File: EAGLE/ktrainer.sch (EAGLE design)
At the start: 10 parts

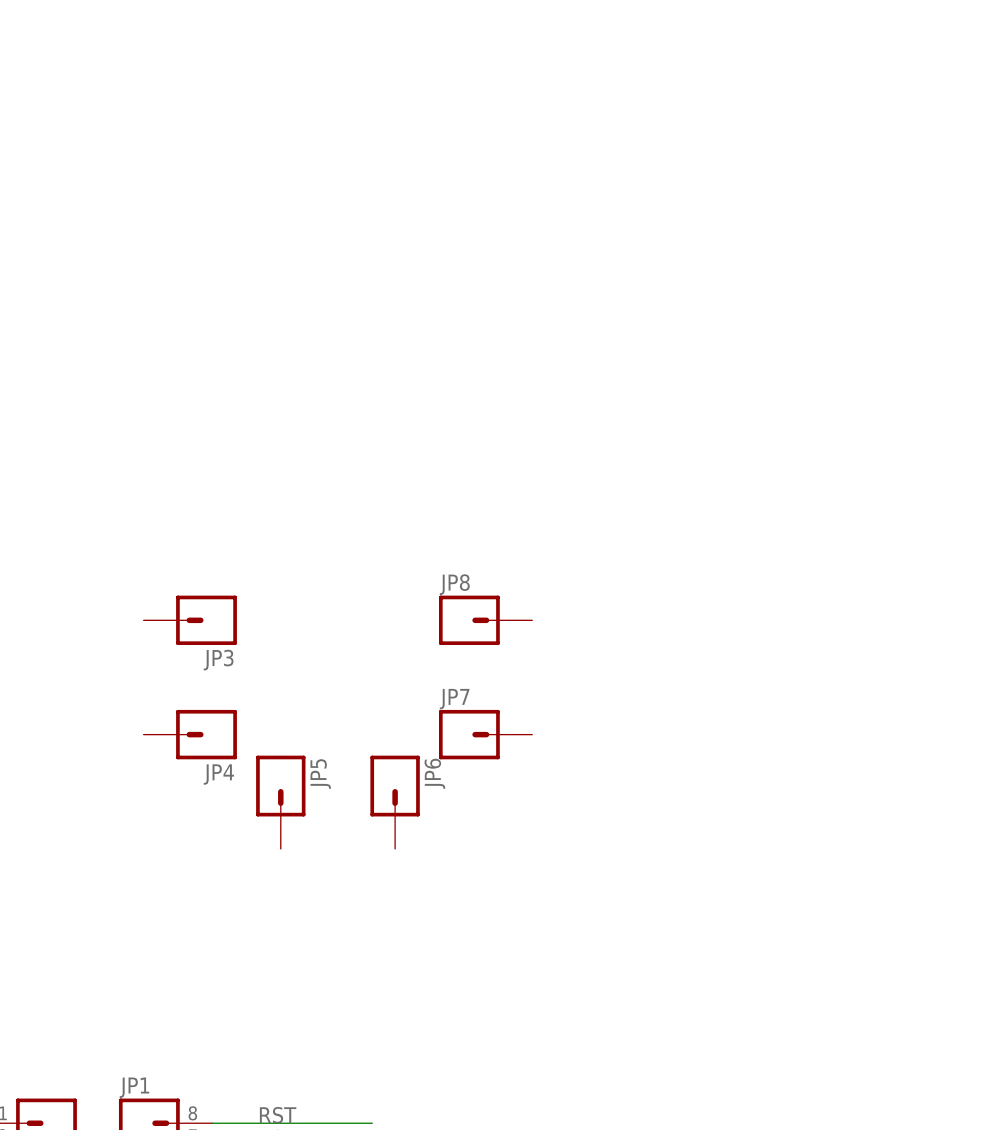
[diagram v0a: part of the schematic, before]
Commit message: First thoughts on the physical layout of buttons & screen
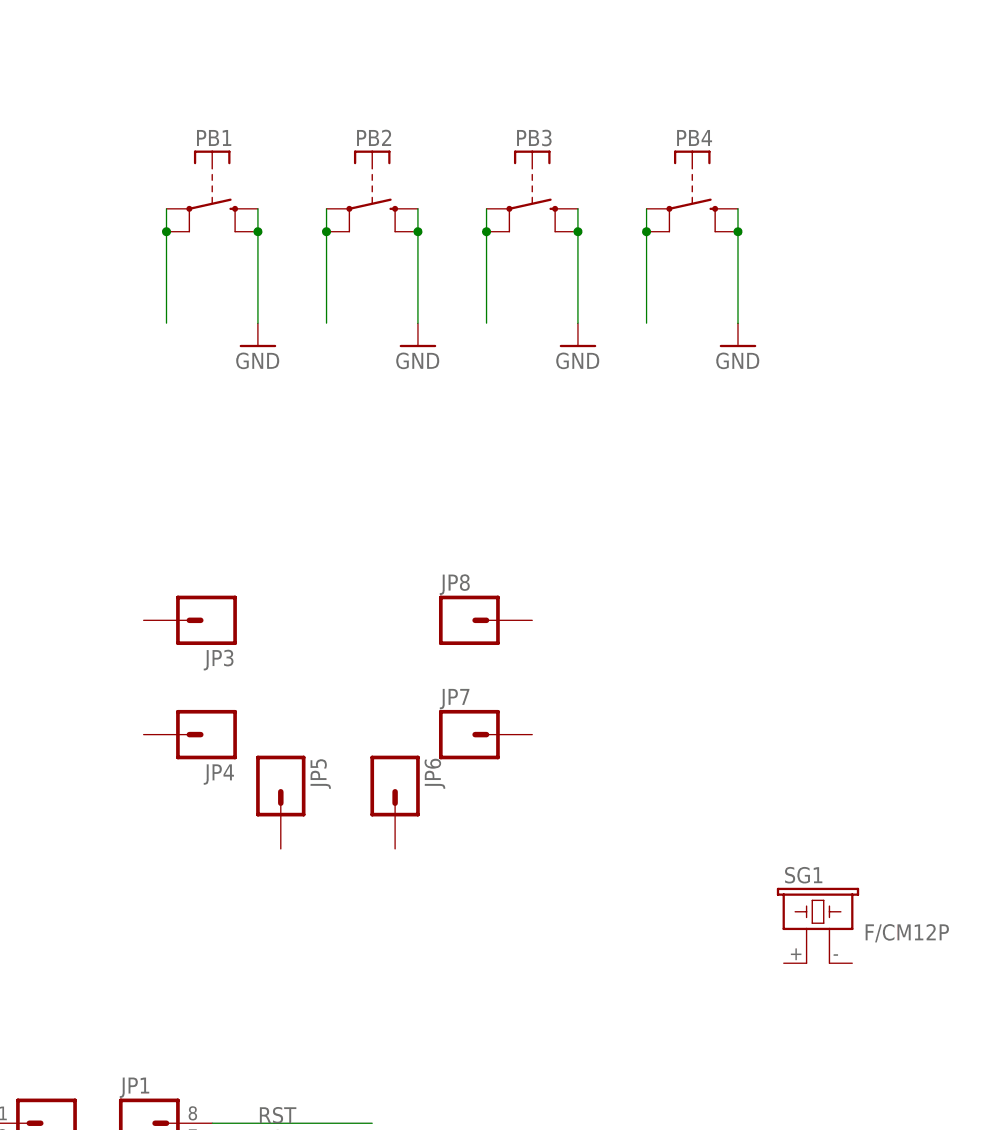
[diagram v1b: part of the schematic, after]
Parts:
- added PB1, PB2, PB3, PB4: SWITCH-SKRA, formatc1702-switches:SWITCH-SKRA
- added SG1: F/CM12P, buzzer:F/CM12P
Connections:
- new net N$1: PB1.S, PB1.S@1
- new net N$2: PB2.S, PB2.S@1
- new net N$3: PB3.S, PB3.S@1
- new net N$4: PB4.S, PB4.S@1
- net GND: now also PB1.P, PB1.P@1, PB2.P, PB2.P@1, PB3.P, PB3.P@1, PB4.P, PB4.P@1
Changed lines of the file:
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@@
 <?xml version="1.0" encoding="utf-8"?>
 <!DOCTYPE eagle SYSTEM "eagle.dtd">
-<eagle version="7.4.0">
+<eagle version="6.5.0">
 <drawing>
 <settings>
@@
 <part name="JP8" library="SparkFun-Connectors" deviceset="M01" device="NOSILK-KIT"/>
 <part name="JP9" library="SparkFun-Connectors" deviceset="M01" device="NOSILK-KIT"/>
+<part name="PB1" library="formatc1702-switches" deviceset="SWITCH-SKRA" device=""/>
+<part name="PB2" library="formatc1702-switches" deviceset="SWITCH-SKRA" device=""/>
+<part name="PB3" library="formatc1702-switches" deviceset="SWITCH-SKRA" device=""/>
+<part name="PB4" library="formatc1702-switches" deviceset="SWITCH-SKRA" device=""/>
+<part name="GND1" library="supply1" deviceset="GND" device=""/>
+<part name="GND2" library="supply1" deviceset="GND" device=""/>
+<part name="GND3" library="supply1" deviceset="GND" device=""/>
+<part name="GND4" library="supply1" deviceset="GND" device=""/>
+<part name="SG1" library="buzzer" deviceset="F/CM12P" device=""/>
 </parts>
 <sheets>
@@
 <attribute name="VALUE" x="43.18" y="58.42" size="1.778" layer="96" rot="R180"/>
 </instance>
+<instance part="PB1" gate="G$1" x="58.42" y="182.88"/>
+<instance part="PB2" gate="G$1" x="76.2" y="182.88"/>
+<instance part="PB3" gate="G$1" x="93.98" y="182.88"/>
+<instance part="PB4" gate="G$1" x="111.76" y="182.88"/>
+<instance part="GND1" gate="1" x="63.5" y="167.64"/>
+<instance part="GND2" gate="1" x="81.28" y="167.64"/>
+<instance part="GND3" gate="1" x="99.06" y="167.64"/>
+<instance part="GND4" gate="1" x="116.84" y="167.64"/>
+<instance part="SG1" gate="G$1" x="124.46" y="101.6"/>
 </instances>
 <busses>
@@
 <label x="20.32" y="66.04" size="1.778" layer="95"/>
 </segment>
+<segment>
+<pinref part="PB1" gate="G$1" pin="P"/>
+<wire x1="63.5" y1="182.88" x2="63.5" y2="180.34" width="0.1524" layer="91"/>
+<pinref part="GND1" gate="1" pin="GND"/>
+<pinref part="PB1" gate="G$1" pin="P@1"/>
+<wire x1="63.5" y1="180.34" x2="63.5" y2="170.18" width="0.1524" layer="91"/>
+<junction x="63.5" y="180.34"/>
+</segment>
+<segment>
+<pinref part="PB2" gate="G$1" pin="P"/>
+<wire x1="81.28" y1="182.88" x2="81.28" y2="180.34" width="0.1524" layer="91"/>
+<pinref part="GND2" gate="1" pin="GND"/>
+<pinref part="PB2" gate="G$1" pin="P@1"/>
+<wire x1="81.28" y1="180.34" x2="81.28" y2="170.18" width="0.1524" layer="91"/>
+<junction x="81.28" y="180.34"/>
+</segment>
+<segment>
+<pinref part="PB3" gate="G$1" pin="P"/>
+<wire x1="99.06" y1="182.88" x2="99.06" y2="180.34" width="0.1524" layer="91"/>
+<pinref part="GND3" gate="1" pin="GND"/>
+<pinref part="PB3" gate="G$1" pin="P@1"/>
+<wire x1="99.06" y1="180.34" x2="99.06" y2="170.18" width="0.1524" layer="91"/>
+<junction x="99.06" y="180.34"/>
+</segment>
+<segment>
+<pinref part="PB4" gate="G$1" pin="P"/>
+<wire x1="116.84" y1="182.88" x2="116.84" y2="180.34" width="0.1524" layer="91"/>
+<pinref part="GND4" gate="1" pin="GND"/>
+<pinref part="PB4" gate="G$1" pin="P@1"/>
+<wire x1="116.84" y1="180.34" x2="116.84" y2="170.18" width="0.1524" layer="91"/>
+<junction x="116.84" y="180.34"/>
+</segment>
 </net>
 <net name="D4" class="0">
@@
 </segment>
 </net>
+<net name="N$1" class="0">
+<segment>
+<pinref part="PB1" gate="G$1" pin="S"/>
+<wire x1="53.34" y1="182.88" x2="53.34" y2="180.34" width="0.1524" layer="91"/>
+<pinref part="PB1" gate="G$1" pin="S@1"/>
+<wire x1="53.34" y1="180.34" x2="53.34" y2="170.18" width="0.1524" layer="91"/>
+<junction x="53.34" y="180.34"/>
+</segment>
+</net>
+<net name="N$2" class="0">
+<segment>
+<pinref part="PB2" gate="G$1" pin="S"/>
+<wire x1="71.12" y1="182.88" x2="71.12" y2="180.34" width="0.1524" layer="91"/>
+<pinref part="PB2" gate="G$1" pin="S@1"/>
+<wire x1="71.12" y1="180.34" x2="71.12" y2="170.18" width="0.1524" layer="91"/>
+<junction x="71.12" y="180.34"/>
+</segment>
+</net>
+<net name="N$3" class="0">
+<segment>
+<pinref part="PB3" gate="G$1" pin="S"/>
+<wire x1="88.9" y1="182.88" x2="88.9" y2="180.34" width="0.1524" layer="91"/>
+<pinref part="PB3" gate="G$1" pin="S@1"/>
+<wire x1="88.9" y1="180.34" x2="88.9" y2="170.18" width="0.1524" layer="91"/>
+<junction x="88.9" y="180.34"/>
+</segment>
+</net>
+<net name="N$4" class="0">
+<segment>
+<pinref part="PB4" gate="G$1" pin="S"/>
+<wire x1="106.68" y1="182.88" x2="106.68" y2="180.34" width="0.1524" layer="91"/>
+<pinref part="PB4" gate="G$1" pin="S@1"/>
+<wire x1="106.68" y1="180.34" x2="106.68" y2="170.18" width="0.1524" layer="91"/>
+<junction x="106.68" y="180.34"/>
+</segment>
+</net>

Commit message: Work on schematic/PCB (not finished)
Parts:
- removed JP1_1: (no value), SparkFun-Connectors:M08NO_SILK_FEMALE_PTH
- removed JP2: OLED, SparkFun-Connectors:M04LONGPADS
- removed JP3, JP4, JP5, JP6, JP7, JP8, JP9: (no value), SparkFun-Connectors:M01NOSILK-KIT
- removed SG1: F/CM12P, buzzer:F/CM12P
- added BUZ1: F/CM12P, buzzer:F/CM12P
- added C1, C2: (no value), rcl:C-EUC0805
- added H1, H2, H3, H4: MOUNT-HOLE2.8, holes:MOUNT-HOLE2.8
- added IC1: DS3231/SO, adafruit:DS3231/SO
- added JP10: POLOLU step up/down 3V3, SparkFun-Connectors:M04LONGPADS
- added LED1: WS2812B, WS2812B:WS2812B
- added R1, R2: (no value), rcl:R-EU_R0805
- added S1: (no value), adafruit:EG1218S
- added SJ1: (no value), jumper:SJ2W
- added U$1: TP4056-LIPO-CHG-PCB, formatc1702-pcbs:TP4056-LIPO-CHG-PCB
- added U$2: SSD1306-OLED-128X64-I2C, formatc1702-pcbs:SSD1306-OLED-128X64-I2C
- added UC1: Wemos D1 mini Pro, esp8266modules:WEMOS-D1-MINI
- JP1: value Wemos D1 mini pro -> (none); device SparkFun-Connectors:M08NO_SILK_FEMALE_PTH -> pinhead:PINHD-1X2
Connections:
- removed net 3V3: JP1.1
- removed net 5V_USB: JP9.1
- removed net A0: JP1.7
- removed net D0: JP1.6
- removed net D1: JP1_1.3
- removed net D2: JP1_1.4
- removed net D3: JP1_1.5
- removed net D4: JP1_1.6
- removed net D5: JP1.5
- removed net D6: JP1.4
- removed net D7: JP1.3
- removed net D8: JP1.2
- removed net N$1: PB1.S, PB1.S@1
- removed net N$2: PB2.S, PB2.S@1
- removed net N$3: PB3.S, PB3.S@1
- removed net N$4: PB4.S, PB4.S@1
- removed net RST: JP1.8
- removed net RX: JP1_1.2
- removed net TX: JP1_1.1
- removed net V_IN: JP1_1.8
- new net +3V3: C1.1, IC1.VCC, JP10.1, LED1.VDD, U$2.VCC, UC1.3V3
- new net +5V: U$1.IN+, UC1.5V
- new net BATSENS: R1.1, R2.2, UC1.A0
- new net BUZZER: BUZ1.1, UC1.D7
- new net LED: LED1.DI, UC1.D6
- new net N$5: JP1.1, U$1.B+
- new net N$6: JP1.2, U$1.B-
- new net N$7: C2.1, IC1.VBAT, SJ1.2
- new net N$8: JP10.3, S1.S
- new net PB1: PB1.S, PB1.S@1, UC1.D1
- new net PB2: PB2.S, PB2.S@1, UC1.D2
- new net PB3: PB3.S, PB3.S@1, UC1.D3
- new net PB4: PB4.S, PB4.S@1, UC1.D4
- new net SCL: IC1.SCL, U$2.SCL, UC1.D5
- new net SDA: IC1.SDA, U$2.SDA, UC1.D0
- new net SHDN: JP10.4
- new net VCC: R1.2, S1.P, U$1.OUT+
- net GND: now also BUZ1.2, C1.2, C2.2, IC1.GND, JP10.2, LED1.GND, R2.1, SJ1.3, U$1.IN-, U$1.OUT-, U$2.GND, UC1.GND; no longer JP1_1.7

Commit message: More work on schematic/PCB (not finished)
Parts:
- removed BUZ1: F/CM12P, buzzer:F/CM12P
- removed H1, H2, H3, H4: MOUNT-HOLE2.8, holes:MOUNT-HOLE2.8
- removed JP10: POLOLU step up/down 3V3, SparkFun-Connectors:M04LONGPADS
- added BUZ+, BUZ-: (no value), wirepad:SMD2
- added JP2: (no value), pinhead:PINHD-1X2
- added U$3: POLOLU-S7V8F3-3V3-STEP-UP-DOWN, formatc1702-pcbs:POLOLU-S7V8F3-3V3-STEP-UP-DOWN
- C1, C2: value (none) -> 100n
- S1: value (none) -> SWITCH-MSK12D04-SLIDER-SMD; device adafruit:EG1218S -> formatc1702-switches:SWITCH-MSK12D04-SLIDER-SMD
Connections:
- net N$7 renamed VBAT
- removed net BUZZER: BUZ1.1, UC1.D7
- removed net N$5: JP1.1, U$1.B+
- removed net SHDN: JP10.4
- new net AUX: JP2.1, UC1.D1
- new net BUZ: BUZ+.P, UC1.D0
- net +3V3: now also U$3.VOUT; no longer JP10.1
- net GND: now also BUZ-.P, JP2.2, U$3.GND; no longer BUZ1.2, JP10.2
- net LED: now also UC1.D4; no longer UC1.D6
- net N$8: now also S1.O, U$3./SHDN, U$3.VIN; no longer JP10.3, S1.S
- net PB1: now also UC1.D7; no longer UC1.D1
- net PB2: now also UC1.D8; no longer UC1.D2
- net PB4: now also UC1.D2; no longer UC1.D4
- net SCL: now also UC1.D6; no longer UC1.D5
- net SDA: now also UC1.D5; no longer UC1.D0
- net VCC: now also JP1.1, SJ1.1, U$1.B+
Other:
- note added: "RETHINK THIS... Remove Wemos regulator? OUTDATED: Cut D2 diode on Wemos D1 mini pro (between VBUS (USB) and +5V traces) https://www.wemos.cc/sites/default/files/2016-09/mini_pro.pdf Attach: Wemos VBUS --> 5V_USB pin (next to Wemos +5V) Wemos +5V pin --> V_IN pin (3.7V from LiPo)"
- note removed: "Cut D2 diode on Wemos D1 mini pro (between VBUS (USB) and +5V traces) https://www.wemos.cc/sites/default/files/2016-09/mini_pro.pdf Attach: Wemos VBUS --> 5V_USB pin (next to Wemos +5V) Wemos +5V pin --> V_IN pin (3.7V from LiPo)"

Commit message: Make PCB fully SMD (only vias, no through-hole pads)
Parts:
- removed JP2: (no value), pinhead:PINHD-1X2
- added TP-AUX, TP-AUX-GND: (no value), wirepad:SMD2
- U$1: value TP4056-LIPO-CHG-PCB -> TP4056-LIPO-CHG-PCBTP4056-PCB-SMD; device formatc1702-pcbs:TP4056-LIPO-CHG-PCB -> formatc1702-pcbs:TP4056-LIPO-CHG-PCBTP4056-PCB-SMD
- U$2: value SSD1306-OLED-128X64-I2C -> SSD1306-OLED-128X64-I2CSSD1306-OLED-128X64-SMD; device formatc1702-pcbs:SSD1306-OLED-128X64-I2C -> formatc1702-pcbs:SSD1306-OLED-128X64-I2CSSD1306-OLED-128X64-SMD
- U$3: value POLOLU-S7V8F3-3V3-STEP-UP-DOWN -> POLOLU-S7V8F3-3V3-STEP-UP-DOWNPOLOLU-S7V8F3-PAD; device formatc1702-pcbs:POLOLU-S7V8F3-3V3-STEP-UP-DOWN -> formatc1702-pcbs:POLOLU-S7V8F3-3V3-STEP-UP-DOWNPOLOLU-S7V8F3-PAD
- UC1: device esp8266modules:WEMOS-D1-MINI -> formatc1702-pcbs:WEMOS-D1-MINIWEMOS-D1-MINI-SMD
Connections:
- net AUX: now also TP-AUX.P; no longer JP2.1
- net GND: now also TP-AUX-GND.P; no longer JP2.2
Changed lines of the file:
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@@
 <part name="LED1" library="WS2812B" deviceset="WS2812B" device=""/>
 <part name="IC1" library="adafruit" deviceset="DS3231" device="/SO"/>
-<part name="U$1" library="formatc1702-pcbs" deviceset="TP4056-LIPO-CHG-PCB" device=""/>
-<part name="UC1" library="esp8266modules" deviceset="WEMOS-D1-MINI" device="" value="Wemos D1 mini Pro"/>
+<part name="U$1" library="formatc1702-pcbs" deviceset="TP4056-LIPO-CHG-PCB" device="TP4056-PCB-SMD" value="TP4056-LIPO-CHG-PCBTP4056-PCB-SMD"/>
+<part name="UC1" library="formatc1702-pcbs" deviceset="WEMOS-D1-MINI" device="WEMOS-D1-MINI-SMD" value="Wemos D1 mini Pro"/>
 <part name="+3V1" library="supply1" deviceset="+3V3" device=""/>
 <part name="+3V2" library="supply1" deviceset="+3V3" device=""/>
@@
 <part name="GND16" library="supply1" deviceset="GND" device=""/>
 <part name="P+3" library="supply1" deviceset="VCC" device=""/>
-<part name="U$2" library="formatc1702-pcbs" deviceset="SSD1306-OLED-128X64-I2C" device=""/>
-<part name="U$3" library="formatc1702-pcbs" deviceset="POLOLU-S7V8F3-3V3-STEP-UP-DOWN" device=""/>
+<part name="U$2" library="formatc1702-pcbs" deviceset="SSD1306-OLED-128X64-I2C" device="SSD1306-OLED-128X64-SMD" value="SSD1306-OLED-128X64-I2CSSD1306-OLED-128X64-SMD"/>
+<part name="U$3" library="formatc1702-pcbs" deviceset="POLOLU-S7V8F3-3V3-STEP-UP-DOWN" device="POLOLU-S7V8F3-PAD" value="POLOLU-S7V8F3-3V3-STEP-UP-DOWNPOLOLU-S7V8F3-PAD"/>
 <part name="S1" library="formatc1702-switches" deviceset="SWITCH-MSK12D04-SLIDER-SMD" device="" value=""/>
 <part name="BUZ+" library="wirepad" deviceset="SMD2" device=""/>
 <part name="BUZ-" library="wirepad" deviceset="SMD2" device=""/>
-<part name="JP2" library="pinhead" deviceset="PINHD-1X2" device=""/>
 <part name="GND17" library="supply1" deviceset="GND" device=""/>
+<part name="TP-AUX" library="wirepad" deviceset="SMD2" device=""/>
+<part name="TP-AUX-GND" library="wirepad" deviceset="SMD2" device=""/>
 </parts>
 <sheets>
@@
 <instance part="BUZ+" gate="1" x="15.24" y="172.72" rot="R270"/>
 <instance part="BUZ-" gate="1" x="30.48" y="172.72" rot="R270"/>
-<instance part="JP2" gate="G$1" x="96.52" y="149.86" rot="MR0"/>
 <instance part="GND17" gate="1" x="106.68" y="139.7"/>
+<instance part="TP-AUX" gate="1" x="96.52" y="152.4"/>
+<instance part="TP-AUX-GND" gate="1" x="96.52" y="149.86"/>
 </instances>
 <busses>
@@
 </segment>
 <segment>
-<pinref part="JP2" gate="G$1" pin="2"/>
 <wire x1="99.06" y1="149.86" x2="106.68" y2="149.86" width="0.1524" layer="91"/>
 <wire x1="106.68" y1="149.86" x2="106.68" y2="142.24" width="0.1524" layer="91"/>
 <pinref part="GND17" gate="1" pin="GND"/>
+<pinref part="TP-AUX-GND" gate="1" pin="P"/>
 </segment>
 </net>
@@
 <net name="AUX" class="0">
 <segment>
-<pinref part="JP2" gate="G$1" pin="1"/>
 <wire x1="99.06" y1="152.4" x2="116.84" y2="152.4" width="0.1524" layer="91"/>
 <label x="114.3" y="152.4" size="1.778" layer="95"/>
-</segment>
-<segment>
+<pinref part="TP-AUX" gate="1" pin="P"/>
+</segment>
+<segment>
